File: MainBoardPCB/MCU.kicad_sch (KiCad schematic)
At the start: 82 parts, among them J1 DX07S016JA1R1500, J1 Micro_SD_Card_Det_Hirose_DM3AT, J4 Conn_02x07_Odd_Even, SW1 SW_Push, SW2 SW_Push, SW3 RESET, SW4 BOOT0, U1 STM32F723IETx, U2 USB6B1, U3 MX25L3233FM1, Y201 12MHz

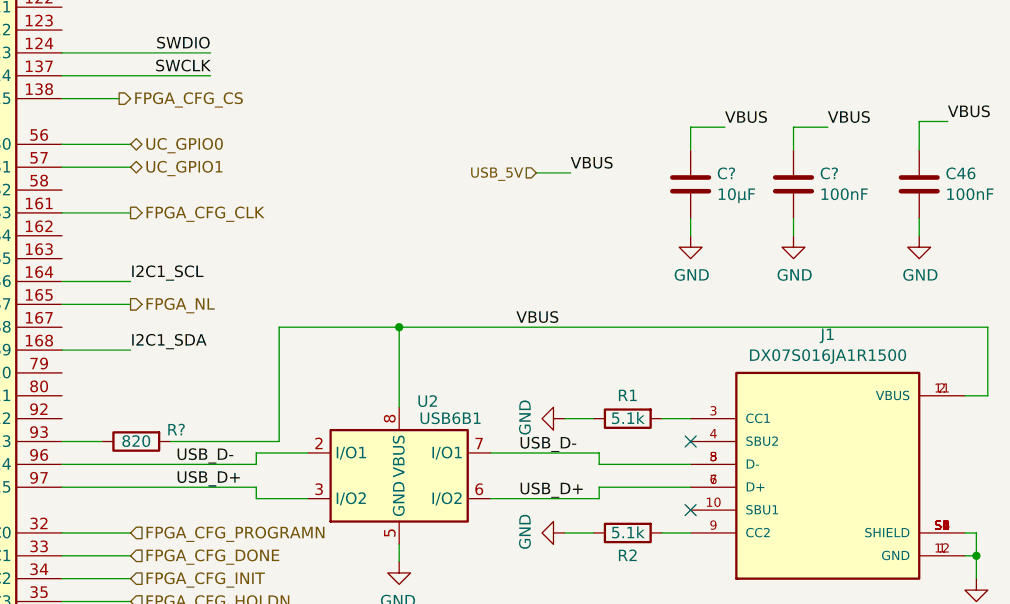
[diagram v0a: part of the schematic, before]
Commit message: Fixes mistake in 1.0, FPGA boot cgf was forced into Master SPI mode
Just make it configurable with pull down resistors.

Signed-off-by: Alexis Jeandet <alexis.jeandet@member.fsf.org>
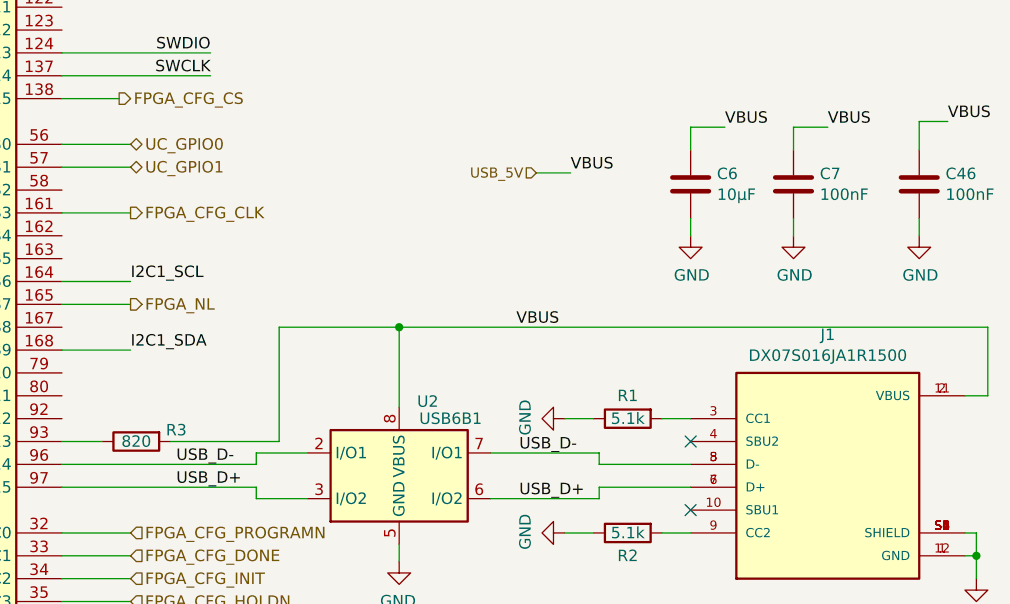
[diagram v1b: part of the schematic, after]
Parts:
- gave numbers to parts that had none: 3
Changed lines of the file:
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@@
 		(instances
 			(project "STicky"
-				(path "/65abeee2-2af2-4609-8a10-d716702626eb/00000000-0000-0000-0000-00005f674c0e"
-					(reference "#PWR?")
+				(path "/65abeee2-2af2-4609-8a10-d716702626eb/00000000-0000-0000-0000-00005f66ca66"
+					(reference "#PWR0161")
 					(unit 1)
 				)
@@
 					(unit 1)
 				)
-				(path "/65abeee2-2af2-4609-8a10-d716702626eb/00000000-0000-0000-0000-00005f66ca66"
-					(reference "#PWR0161")
+				(path "/65abeee2-2af2-4609-8a10-d716702626eb/00000000-0000-0000-0000-00005f674c0e"
+					(reference "#PWR?")
 					(unit 1)
 				)
@@
 		(instances
 			(project "STicky"
-				(path "/65abeee2-2af2-4609-8a10-d716702626eb/00000000-0000-0000-0000-00005f674c0e"
-					(reference "#PWR?")
+				(path "/65abeee2-2af2-4609-8a10-d716702626eb/00000000-0000-0000-0000-00005f66ca66"
+					(reference "#PWR0152")
 					(unit 1)
 				)
@@
 					(unit 1)
 				)
-				(path "/65abeee2-2af2-4609-8a10-d716702626eb/00000000-0000-0000-0000-00005f66ca66"
-					(reference "#PWR0152")
+				(path "/65abeee2-2af2-4609-8a10-d716702626eb/00000000-0000-0000-0000-00005f674c0e"
+					(reference "#PWR?")
 					(unit 1)
 				)
@@
 		(instances
 			(project "STicky"
-				(path "/65abeee2-2af2-4609-8a10-d716702626eb/00000000-0000-0000-0000-00005f674c0e"
-					(reference "R?")
+				(path "/65abeee2-2af2-4609-8a10-d716702626eb/00000000-0000-0000-0000-00005f66ca66"
+					(reference "R3")
 					(unit 1)
 				)
@@
 					(unit 1)
 				)
-				(path "/65abeee2-2af2-4609-8a10-d716702626eb/00000000-0000-0000-0000-00005f66ca66"
-					(reference "R3")
+				(path "/65abeee2-2af2-4609-8a10-d716702626eb/00000000-0000-0000-0000-00005f674c0e"
+					(reference "R?")
 					(unit 1)
 				)
@@
 		(instances
 			(project "STicky"
-				(path "/65abeee2-2af2-4609-8a10-d716702626eb/00000000-0000-0000-0000-00005f674c0e"
-					(reference "#PWR?")
+				(path "/65abeee2-2af2-4609-8a10-d716702626eb/00000000-0000-0000-0000-00005f66ca66"
+					(reference "#PWR0153")
 					(unit 1)
 				)
@@
 					(unit 1)
 				)
-				(path "/65abeee2-2af2-4609-8a10-d716702626eb/00000000-0000-0000-0000-00005f66ca66"
-					(reference "#PWR0153")
+				(path "/65abeee2-2af2-4609-8a10-d716702626eb/00000000-0000-0000-0000-00005f674c0e"
+					(reference "#PWR?")
 					(unit 1)
 				)
@@
 		(instances
 			(project "STicky"
-				(path "/65abeee2-2af2-4609-8a10-d716702626eb/00000000-0000-0000-0000-00005f674c0e"
-					(reference "C?")
+				(path "/65abeee2-2af2-4609-8a10-d716702626eb/00000000-0000-0000-0000-00005f66ca66"
+					(reference "C6")
 					(unit 1)
 				)
@@
 					(unit 1)
 				)
-				(path "/65abeee2-2af2-4609-8a10-d716702626eb/00000000-0000-0000-0000-00005f66ca66"
-					(reference "C6")
+				(path "/65abeee2-2af2-4609-8a10-d716702626eb/00000000-0000-0000-0000-00005f674c0e"
+					(reference "C?")
 					(unit 1)
 				)
@@
 		(instances
 			(project "STicky"
-				(path "/65abeee2-2af2-4609-8a10-d716702626eb/00000000-0000-0000-0000-00005f674c0e"
-					(reference "#PWR?")
+				(path "/65abeee2-2af2-4609-8a10-d716702626eb/00000000-0000-0000-0000-00005f66ca66"
+					(reference "#PWR0154")
 					(unit 1)
 				)
@@
 					(unit 1)
 				)
-				(path "/65abeee2-2af2-4609-8a10-d716702626eb/00000000-0000-0000-0000-00005f66ca66"
-					(reference "#PWR0154")
+				(path "/65abeee2-2af2-4609-8a10-d716702626eb/00000000-0000-0000-0000-00005f674c0e"
+					(reference "#PWR?")
 					(unit 1)
 				)
@@
 		(instances
 			(project "STicky"
-				(path "/65abeee2-2af2-4609-8a10-d716702626eb/00000000-0000-0000-0000-00005f674c0e"
-					(reference "C?")
+				(path "/65abeee2-2af2-4609-8a10-d716702626eb/00000000-0000-0000-0000-00005f66ca66"
+					(reference "C7")
 					(unit 1)
 				)
@@
 					(unit 1)
 				)
-				(path "/65abeee2-2af2-4609-8a10-d716702626eb/00000000-0000-0000-0000-00005f66ca66"
-					(reference "C7")
+				(path "/65abeee2-2af2-4609-8a10-d716702626eb/00000000-0000-0000-0000-00005f674c0e"
+					(reference "C?")
 					(unit 1)
 				)

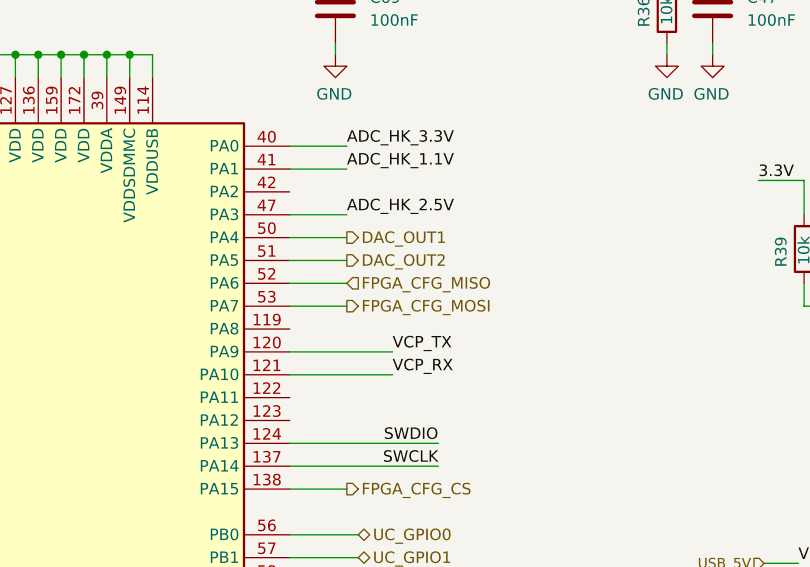
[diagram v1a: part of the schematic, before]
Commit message: Fixes FPGA CFG slave serial interface wiring
Signed-off-by: Alexis Jeandet <alexis.jeandet@member.fsf.org>
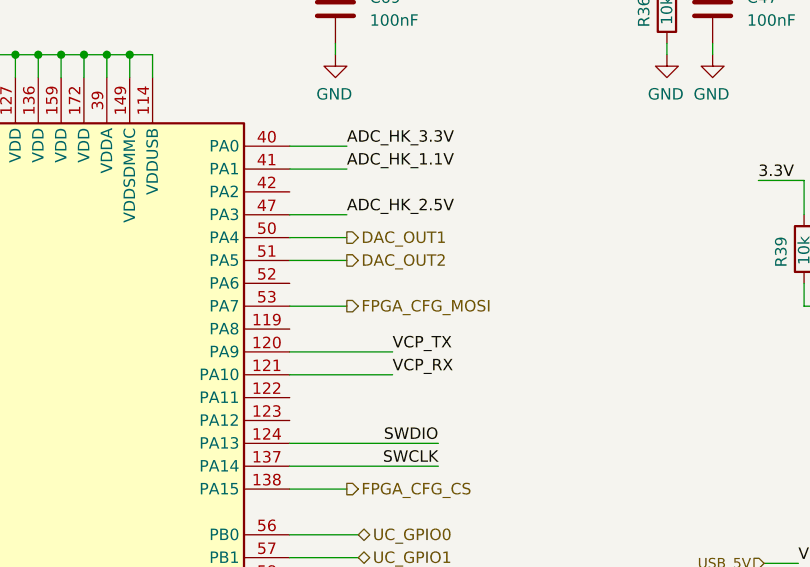
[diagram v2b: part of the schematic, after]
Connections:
- net FPGA_CFG_MISO: no longer names the net of U1.52 (PA6)
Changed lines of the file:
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@@
 	(wire
 		(pts
-			(xy 299.72 53.34) (xy 306.07 53.34)
-		)
-		(stroke
-			(width 0)
-			(type default)
-		)
-	)
-	(wire
-		(pts
 			(xy 170.18 115.57) (xy 170.18 116.84)
 		)
@@
 		)
 	)
-	(hierarchical_label "FPGA_CFG_MISO"
-		(shape input)
-		(at 306.07 53.34 0)
-		(fields_autoplaced yes)
-		(effects
-			(font
-				(size 1.27 1.27)
-			)
-			(justify left)
-		)
-	)
 	(hierarchical_label "FPGA_IO2"
 		(shape bidirectional)
@@
 		(on_board yes)
 		(dnp no)
-		(property "Reference" "#PWR?"
+		(property "Reference" "#PWR0161"
 			(at 85.09 199.39 0)
 			(effects
@@
 		(on_board yes)
 		(dnp no)
-		(property "Reference" "#PWR?"
+		(property "Reference" "#PWR0152"
 			(at 369.57 97.79 0)
 			(effects
@@
 		(on_board yes)
 		(dnp no)
-		(property "Reference" "R?"
+		(property "Reference" "R3"
 			(at 312.42 113.03 90)
 			(effects
@@
 		(on_board yes)
 		(dnp no)
-		(property "Reference" "#PWR?"
+		(property "Reference" "#PWR0153"
 			(at 381 97.79 0)
 			(effects
@@
 		(on_board yes)
 		(dnp no)
-		(property "Reference" "C?"
+		(property "Reference" "C6"
 			(at 372.491 84.5566 0)
 			(effects
@@
 		(on_board yes)
 		(dnp no)
-		(property "Reference" "#PWR?"
+		(property "Reference" "#PWR0154"
 			(at 337.185 133.985 0)
 			(effects
@@
 		(on_board yes)
 		(dnp no)
-		(property "Reference" "C?"
+		(property "Reference" "C7"
 			(at 383.921 84.5566 0)
 			(effects

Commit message: New Fusion main board version using a more beefy MCU.
Signed-off-by: Alexis Jeandet <alexis.jeandet@member.fsf.org>
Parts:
- removed C10, C11, C205, C209, C3, C4, C7: 100nF, Capacitor_SMD:C_0402_1005Metric, symbol Device:C
- removed C2, C210: 2.2µF, Capacitor_SMD:C_1206_3216Metric_Pad1.33x1.80mm_HandSolder, symbol Device:C
- removed C37, C41, C42, C43, C44, C45: 10nF, Capacitor_SMD:C_0402_1005Metric_Pad0.74x0.62mm_HandSolder, symbol Device:C
- removed C47, C48, C69: 100nF, Capacitor_SMD:C_0402_1005Metric_Pad0.74x0.62mm_HandSolder, symbol Device:C
- removed C6: 10µF, Capacitor_SMD:C_1206_3216Metric_Pad1.33x1.80mm_HandSolder, symbol Device:C
- removed R15, R21, R22, R23, R24, R25: 1k, Resistor_SMD:R_0402_1005Metric_Pad0.72x0.64mm_HandSolder, symbol Device:R
- removed R19: 10k, Resistor_SMD:R_0402_1005Metric, symbol Device:R
- removed R35, R36, R37, R41: 10k, Resistor_SMD:R_0402_1005Metric_Pad0.72x0.64mm_HandSolder, symbol Device:R
- removed R5, R8, R9: 100k, Resistor_SMD:R_0402_1005Metric, symbol Device:R
- removed R6: 3K, Resistor_SMD:R_0402_1005Metric, symbol Device:R
- removed U1: STM32F723IETx, Package_QFP:LQFP-176_24x24mm_P0.5mm, symbol MCU_ST_STM32F7:STM32F723IETx
- added C217, C223, C225, C227: 1µF, Capacitor_SMD:C_1206_3216Metric_Pad1.33x1.80mm_HandSolder, symbol Device:C
- added C219, C220, C224, C226, C228, C229, C230: 100nF, Capacitor_SMD:C_0402_1005Metric, symbol Device:C
- added C222: 2.2µF, Capacitor_SMD:C_1206_3216Metric_Pad1.33x1.80mm_HandSolder, symbol Device:C
- added JP201: SolderJumper_2_Open, Jumper:SolderJumper-2_P1.3mm_Open_TrianglePad1.0x1.5mm, symbol Jumper:SolderJumper_2_Open
- added U203: STM32H7S3Z8Tx, Package_QFP:LQFP-144_20x20mm_P0.5mm, symbol MCU_ST_STM32H7:STM32H7S3Z8Tx
- renumbered C13 to C201, C14 to C202, C51 to C203, C5 to C204, C9 to C205, C211 to C207, C212 to C208, C207 to C209, C208 to C210, C1 to C211, C2 to C212, C12 to C213, C1 to C214, C46 to C215, C201 to C216, C204 to C218, C8 to C221, D2 to D201, D1 to D202, J4 to J201, J1 to J202, J1 to J203, R7 to R201, R4 to R202, R201 to R203, R202 to R204, R203 to R205, R14 to R206, R20 to R207, R38 to R208, R2 to R209, R1 to R210, R1 to R211, R2 to R212, R3 to R213, R204 to R214, R205 to R215, R39 to R216, R40 to R217, SW1 to SW201, SW2 to SW202, SW4 to SW203, SW3 to SW204, U3 to U201, U2 to U202
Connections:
- net 3.3V: now also C217.1, C219.1, C223.1, C224.1, C225.1, C226.1, JP201.1 (A), U203.100 (VDD), U203.108 (VDD), U203.115 (VDD50USB), U203.116 (VDD33USB), U203.123 (VDD), U203.133 (VDD), U203.139 (VDD), U203.17 (VDD), U203.24 (VREFP), U203.25 (VDDA), U203.31 (VDD), U203.41 (VDD), U203.69 (VDD), U203.7 (VDD), U203.81 (VDD), U203.88 (VDD); no longer C221.1
- net BOOT0: now also U203.128 (BOOT0)
- net CARD_DETECT: now also U203.129 (PD5)
- net FPGA_A0: now also U203.19 (PC1)
- net FPGA_A1: now also U203.20 (PC2)
- net FPGA_A2: now also U203.21 (PC3)
- net FPGA_CFG_CLK: now also U203.101 (PC10)
- net FPGA_CFG_DONE: now also U203.54 (PP5)
- net FPGA_CFG_INIT: now also U203.55 (PP0)
- net FPGA_CFG_MOSI: now also U203.103 (PC12)
- net FPGA_CFG_PROGRAMN: now also U203.53 (PO4)
- net FPGA_CLK: now also U203.67 (PD10)
- net FPGA_D0: now also U203.94 (PA12)
- net FPGA_D1: now also U203.93 (PA11)
- net FPGA_D10: now also U203.74 (PB11)
- net FPGA_D11: now also U203.73 (PB10)
- net FPGA_D12: now also U203.9 (PE3)
- net FPGA_D13: now also U203.10 (PE4)
- net FPGA_D14: now also U203.11 (PE5)
- net FPGA_D15: now also U203.12 (PE6)
- net FPGA_D2: now also U203.92 (PA10)
- net FPGA_D3: now also U203.91 (PA9)
- net FPGA_D4: now also U203.90 (PA8)
- net FPGA_D5: now also U203.28 (PA2)
- net FPGA_D6: now also U203.27 (PA1)
- net FPGA_D7: now also U203.26 (PA0)
- net FPGA_D8: now also U203.76 (PB13)
- net FPGA_D9: now also U203.75 (PB12)
- net FPGA_HAVE_DATA: now also U203.82 (PD14)
- net FPGA_NE1: now also U203.71 (PD12)
- net FPGA_NL: now also U203.110 (PD4)
- net FPGA_NOE: now also U203.39 (PB1)
- net FPGA_NWAIT: now also U203.109 (PD3)
- net FPGA_NWE: now also U203.40 (PB2)
- net GND: now also C217.2, C219.2, C220.2, C222.2, C223.2, C224.2, C225.2, C226.2, C227.1, C228.1, C229.1, C230.1, U203.107 (VSS), U203.117 (VSSUSB), U203.132 (VSS), U203.138 (VSS), U203.16 (VSS), U203.22 (VSSA), U203.23 (VREFM), U203.30 (VSS), U203.42 (VSS), U203.46 (VSS), U203.50 (VSS), U203.56 (VSS), U203.62 (VSS), U203.70 (VSS), U203.8 (VSS), U203.80 (VSS), U203.89 (VSS), U203.99 (VSS)
- net I2C1_SCL: now also U203.1 (PB8)
- net I2C1_SDA: now also U203.2 (PB9)
- net LED1: now also U203.18 (PC0)
- net LED2: now also U203.6 (PC15)
- net RESET: now also U203.15 (NRST)
- net SDMMC_CLK: now also U203.130 (PD6)
- net SDMMC_CMD: now also U203.131 (PD7)
- net SDMMC_D0: now also U203.77 (PB14)
- net SDMMC_D1: now also U203.78 (PB15)
- net SDMMC_D2: now also U203.134 (PB3(JTDO)
- net SDMMC_D3: now also U203.135 (PB4(NJTRST))
- net SPI5_MISO: now also U203.126 (PM14)
- net SPI5_MOSI: now also U203.127 (PM13)
- net SPI5_NSS: now also U203.124 (PM12)
- net SPI5_SCK: now also U203.125 (PM11)
- net SPI_FLASH_CS: now also U203.32 (PA4)
- net SPI_FLASH_MISO: now also U203.34 (PA6)
- net SPI_FLASH_MOSI: now also U203.35 (PA7)
- net SPI_FLASH_SCK: now also U203.33 (PA5)
- net SWCLK: now also U203.96 (PA14(JTCK)
- net SWDIO: now also U203.95 (PA13(JTMS)
- net UC_GPIO0: now also U203.84 (PC6)
- net UC_GPIO1: now also U203.85 (PC7)
- net USB_D+: now also U203.119 (PM6)
- net USB_D-: now also U203.118 (PM5)
- net USER_BP1: now also U203.5 (PC14)
- net USER_BP2: now also U203.29 (PA3)
- net VCP_RX: now also U203.104 (PD0)
- net VCP_TX: now also U203.105 (PD1)
- net VBUS_SENSE: now reaches R213.1
- net VBUS_SENSE: now also U203.121 (PM8)
- net at Y201.1: now also U203.13 (PH0)
- net at Y201.3: now also U203.14 (PH1)
- net VCap: now reaches C218.1
- net VCap: now also C221.1, C220.1, C222.1, U203.120 (DVDD), U203.137 (VCAP4), U203.43 (VCAP1), U203.79 (VCAP2), U203.98 (VCAP3)
- new net: C227.2, C228.2, C229.2, C230.2, JP201.2 (B), U203.45 (VDDXSPI1), U203.51 (VDDXSPI1), U203.57 (VDDXSPI1), U203.63 (VDDXSPI1)
- new net FPGA_UART2_RX: U203.144 (PB7)
- new net FPGA_UART2_TX: U203.143 (PB6)
- new net FPGA_UART_RX: U203.140 (PE0)
- new net FPGA_UART_TX: U203.141 (PE1)
- new net PSU_Alert: U203.142 (PE2)
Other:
- note added: "FLASH"
- note added: "USB"
- note added: "VDDA"
- note added: "VDDUSB"
- note added: "VREFP"
- note removed: "Analog inputs"
- moved on the sheet: C201, C202, C203, C204, C205, C206, C207, C208, C209, C210, C211, C212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
